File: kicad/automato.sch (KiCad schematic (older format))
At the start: 75 parts, among them J1 USB_C_Receptacle, J10 QWIIC 0, J11 1WIRE 0, J12 1WIRE 1, J2 LiPo, J3 Conn_01x07_Male, J4 Screw_Terminal_01x20, J5 USB_C_Receptacle, J6 Conn_Coaxial, J7 UART2 0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

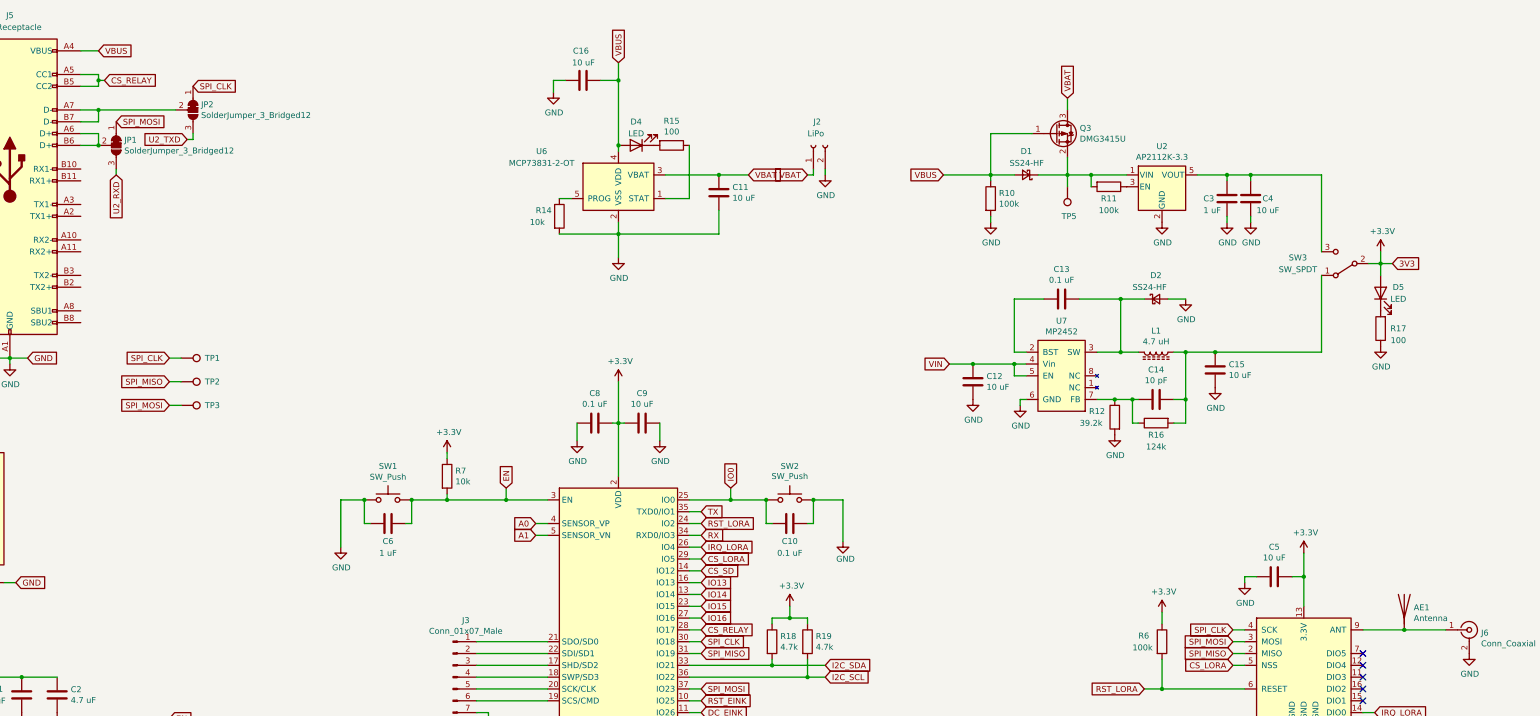
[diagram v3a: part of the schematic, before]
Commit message: move some display pins around, change relay usb-c power to 3v3
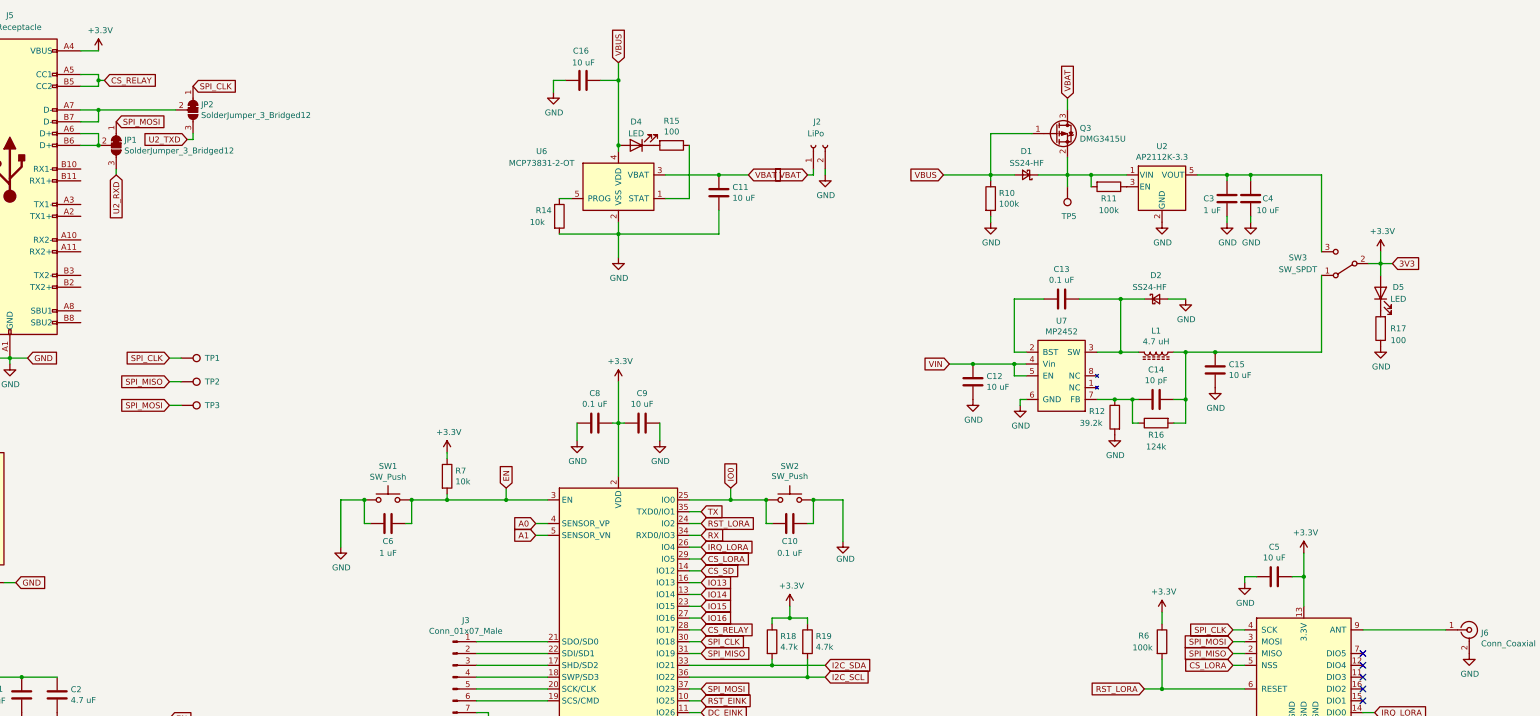
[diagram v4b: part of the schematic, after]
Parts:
- removed AE1: Antenna, Connector_PinHeader_2.54mm:PinHeader_1x01_P2.54mm_Vertical, symbol Device:Antenna
- J3: footprint Connector_PinHeader_2.54mm:PinHeader_1x07_P2.54mm_Horizontal -> Connector_PinHeader_2.54mm:PinHeader_1x07_P2.54mm_Vertical
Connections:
- net +3V3: now also J5.A4 (VBUS), J5.A9 (VBUS), J5.B4 (VBUS), J5.B9 (VBUS)
- net VBUS: no longer J5.A4 (VBUS), J5.A9 (VBUS), J5.B4 (VBUS), J5.B9 (VBUS)
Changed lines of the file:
@@
 Wire Wire Line
 	14250 5450 14250 5400
-Wire Wire Line
-	15250 5850 15600 5850
-$Comp
-L Device:Antenna AE1
-U 1 1 602BF430
-P 15600 5650
-F 0 "AE1" H 15680 5639 50  0000 L CNN
-F 1 "Antenna" H 15680 5548 50  0000 L CNN
-F 2 "Connector_PinHeader_2.54mm:PinHeader_1x01_P2.54mm_Vertical" H 15600 5650 50  0001 C CNN
-F 3 "~" H 15600 5650 50  0001 C CNN
-	1    15600 5650
-	1    0    0    -1
-$EndComp
 Connection ~ 13550 6350
 Wire Wire Line
@@
 F 0 "J3" H 7658 6731 50  0000 C CNN
 F 1 "Conn_01x07_Male" H 7658 6640 50  0000 C CNN
-F 2 "Connector_PinHeader_2.54mm:PinHeader_1x07_P2.54mm_Horizontal" H 7550 6250 50  0001 C CNN
+F 2 "Connector_PinHeader_2.54mm:PinHeader_1x07_P2.54mm_Vertical" H 7550 6250 50  0001 C CNN
 F 3 "~" H 7550 6250 50  0001 C CNN
 	1    7550 6250
@@
 Text GLabel 10350 9800 1    50   Input ~ 0
 VBUS
-Text GLabel 4550 950  2    50   Input ~ 0
-VBUS
 Wire Wire Line
 	4550 950  4400 950
@@
 	1    0    0    -1
 $EndComp
-Wire Wire Line
-	15600 5850 15950 5850
-Connection ~ 15600 5850
 $Comp
 L power:GND #PWR0104
@@
 	0    1    1    0
 $EndComp
+Wire Wire Line
+	15250 5850 15950 5850
+$Comp
+L power:+3.3V #PWR0111
+U 1 1 635475AD
+P 4550 950
+F 0 "#PWR0111" H 4550 800 50  0001 C CNN
+F 1 "+3.3V" H 4565 1123 50  0000 C CNN
+F 2 "" H 4550 950 50  0001 C CNN
+F 3 "" H 4550 950 50  0001 C CNN
+	1    4550 950
+	1    0    0    -1
+$EndComp
 $EndSCHEMATC

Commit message: add stemma connectors
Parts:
- removed J11: 1WIRE 0, symbol Connector:Conn_01x02_Male
- removed J12: 1WIRE 1, symbol Connector:Conn_01x02_Male
- J4: value Screw_Terminal_01x20 -> Screw_Terminal_01x15; footprint automato-sensor:TerminalBlock_Phoenix_PT-1,5-20-3.5-H_1x20_P3.50mm_Horizontal -> TerminalBlock_Phoenix:TerminalBlock_Phoenix_PT-1,5-15-3.5-H_1x15_P3.50mm_Horizontal; symbol Connector:Screw_Terminal_01x20 -> Connector:Screw_Terminal_01x15
- J7, J9: footprint (none) -> Connector_JST:JST_PH_S3B-PH-SM4-TB_1x03-1MP_P2.00mm_Horizontal
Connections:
- net +3V3: now also J4.8 (Pin_8); no longer J4.11 (Pin_11), J4.9 (Pin_9)
- net A0: now also J4.5 (Pin_5); no longer J4.8 (Pin_8)
- net A1: now also J4.4 (Pin_4); no longer J4.7 (Pin_7)
- net A6: now also J4.2 (Pin_2); no longer J4.6 (Pin_6)
- net A7: now also J4.1 (Pin_1); no longer J4.5 (Pin_5)
- net GND: now also J4.10 (Pin_10), J4.14 (Pin_14), J4.3 (Pin_3), J4.6 (Pin_6); no longer J4.13 (Pin_13), J4.17 (Pin_17), J4.20 (Pin_20)
- net I2C_SCL: no longer J4.1 (Pin_1)
- net I2C_SDA: no longer J4.2 (Pin_2)
- net IO13: now also J4.13 (Pin_13); no longer J4.16 (Pin_16)
- net IO14: now also J4.11 (Pin_11); no longer J4.14 (Pin_14)
- net IO15: now also J4.9 (Pin_9); no longer J4.12 (Pin_12)
- net IO16: now also J4.7 (Pin_7); no longer J4.10 (Pin_10)
- net RX: no longer J4.4 (Pin_4)
- net TX: no longer J4.3 (Pin_3)
- net VBAT: no longer J4.18 (Pin_18)
- net VBUS: now also J4.12 (Pin_12); no longer J4.15 (Pin_15)
- net VIN: now also J4.15 (Pin_15); no longer J4.19 (Pin_19)
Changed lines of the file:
@@
 Comment4 ""
 $EndDescr
+Text GLabel 9650 9800 1    50   Input ~ 0
+A6
 Text GLabel 9750 9800 1    50   Input ~ 0
-A6
-Text GLabel 9850 9800 1    50   Input ~ 0
 A7
-Text GLabel 10250 9800 1    50   Input ~ 0
-I2C_SCL
-Text GLabel 10150 9800 1    50   Input ~ 0
-I2C_SDA
-Text GLabel 10050 9800 1    50   Input ~ 0
-TX
-Text GLabel 9950 9800 1    50   Input ~ 0
-RX
 Text GLabel 11400 9650 0    50   Input ~ 0
 SPI_MOSI
@@
 Wire Wire Line
 	12300 3600 12400 3600
-Text GLabel 9550 9800 1    50   Input ~ 0
+Text GLabel 9350 9800 1    50   Input ~ 0
 A0
-Text GLabel 9650 9800 1    50   Input ~ 0
+Text GLabel 9450 9800 1    50   Input ~ 0
 A1
-Text GLabel 8850 9800 1    50   Input ~ 0
+Text GLabel 8650 9800 1    50   Input ~ 0
 VBUS
-Text GLabel 8450 9800 1    50   Input ~ 0
+Text GLabel 8350 9800 1    50   Input ~ 0
 VIN
-Text GLabel 8550 9800 1    50   Input ~ 0
-VBAT
 Text GLabel 1250 3550 2    50   Input ~ 0
 GND
 Wire Wire Line
 	1150 3550 1250 3550
-Text GLabel 8350 9800 1    50   Input ~ 0
+Text GLabel 8450 9800 1    50   Input ~ 0
 GND
-Text GLabel 8650 9800 1    50   Input ~ 0
+Text GLabel 8850 9800 1    50   Input ~ 0
+GND
+Text GLabel 9250 9800 1    50   Input ~ 0
 GND
 Text GLabel 9050 9800 1    50   Input ~ 0
-GND
-Text GLabel 9250 9800 1    50   Input ~ 0
-3V3
-Text GLabel 9450 9800 1    50   Input ~ 0
 3V3
 $Comp
@@
 	3800 3550 3800 3600
 $Comp
-L Connector:Screw_Terminal_01x20 J4
+L Connector:Screw_Terminal_01x15 J4
 U 1 1 60071AD4
-P 9350 10000
-F 0 "J4" V 9475 9946 50  0000 C CNN
-F 1 "Screw_Terminal_01x20" V 9566 9946 50  0000 C CNN
-F 2 "automato-sensor:TerminalBlock_Phoenix_PT-1,5-20-3.5-H_1x20_P3.50mm_Horizontal" H 9350 10000 50  0001 C CNN
-F 3 "~" H 9350 10000 50  0001 C CNN
-	1    9350 10000
-	0    1    1    0
-$EndComp
-Text GLabel 10450 9800 1    50   Input ~ 0
-VBAT
-Text GLabel 10350 9800 1    50   Input ~ 0
-VBUS
+P 9050 10000
+F 0 "J4" V 9175 9946 50  0000 C CNN
+F 1 "Screw_Terminal_01x15" V 9266 9946 50  0000 C CNN
+F 2 "TerminalBlock_Phoenix:TerminalBlock_Phoenix_PT-1,5-15-3.5-H_1x15_P3.50mm_Horizontal" H 9050 10000 50  0001 C CNN
+F 3 "~" H 9050 10000 50  0001 C CNN
+	1    9050 10000
+	0    1    1    0
+$EndComp
 Wire Wire Line
 	4550 950  4400 950
@@
 Wire Wire Line
 	9550 6750 9650 6750
-Text GLabel 9350 9800 1    50   Input ~ 0
+Text GLabel 9150 9800 1    50   Input ~ 0
 IO16
+Text GLabel 8550 9800 1    50   Input ~ 0
+IO13
 Text GLabel 8750 9800 1    50   Input ~ 0
-IO13
+IO14
 Text GLabel 8950 9800 1    50   Input ~ 0
-IO14
-Text GLabel 9150 9800 1    50   Input ~ 0
 IO15
 $Comp
@@
 $EndComp
 $Comp
-L Connector:Conn_01x02_Male J11
-U 1 1 632B9C4F
-P 5500 9450
-F 0 "J11" H 5608 9631 50  0000 C CNN
-F 1 "1WIRE 0" H 5608 9540 50  0000 C CNN
-F 2 "" H 5500 9450 50  0001 C CNN
-F 3 "~" H 5500 9450 50  0001 C CNN
-	1    5500 9450
-	1    0    0    -1
-$EndComp
-$Comp
-L Connector:Conn_01x02_Male J12
-U 1 1 632BAE07
-P 6300 9450
-F 0 "J12" H 6408 9631 50  0000 C CNN
-F 1 "1WIRE 1" H 6408 9540 50  0000 C CNN
-F 2 "" H 6300 9450 50  0001 C CNN
-F 3 "~" H 6300 9450 50  0001 C CNN
-	1    6300 9450
-	1    0    0    -1
-$EndComp
-$Comp
 L Connector:Conn_01x03_Male J7
 U 1 1 632E9370
@@
 F 0 "J7" H 2558 9831 50  0000 C CNN
 F 1 "UART2 0" H 2558 9740 50  0000 C CNN
-F 2 "" H 2450 9550 50  0001 C CNN
+F 2 "Connector_JST:JST_PH_S3B-PH-SM4-TB_1x03-1MP_P2.00mm_Horizontal" H 2450 9550 50  0001 C CNN
 F 3 "~" H 2450 9550 50  0001 C CNN
 	1    2450 9550
@@
 F 0 "J9" H 3358 9831 50  0000 C CNN
 F 1 "UART2 1" H 3358 9740 50  0000 C CNN
-F 2 "" H 3250 9550 50  0001 C CNN
+F 2 "Connector_JST:JST_PH_S3B-PH-SM4-TB_1x03-1MP_P2.00mm_Horizontal" H 3250 9550 50  0001 C CNN
 F 3 "~" H 3250 9550 50  0001 C CNN
 	1    3250 9550
@@
 	1    0    0    -1
 $EndComp
+Text GLabel 9550 9800 1    50   Input ~ 0
+GND
 $EndSCHEMATC
